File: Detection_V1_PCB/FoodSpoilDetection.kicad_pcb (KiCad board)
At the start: 2 copper layers, 60 x 65 mm, 43 parts, among them J1 Conn_01x03_Socket, J2 Conn_01x04_Socket, J3 Conn_01x06_Socket, J4 Conn_01x03_Socket, J5 Conn_01x10_Socket, J6 Conn_01x03_Socket, Q1 AO3401A, Q2 AO3400A, Q3 AO3401A, U1 XIAO-ESP32-S3-DIP

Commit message: swwe
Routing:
- net Net-(D1-K): track 95.0 -> 107.0 mm
- net GNDPWR: track 226.0 -> 221.3 mm
- net GND: vias 4 -> 2
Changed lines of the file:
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@@
+	)
+	(segment
+		(start 126.1 109.9375)
+		(end 126.1 118.205634)
+		(width 0.2)
+		(layer "F.Cu")
+		(net 13)
 	)
 	(segment
@@
 	)
 	(segment
+		(start 126.1 118.205634)
+		(end 126.4 118.505634)
+		(width 0.2)
+		(layer "F.Cu")
+		(net 13)
+	)
+	(segment
 		(start 156.75 101.310835)
 		(end 156.75 105.9829)
@@
 	)
 	(segment
+		(start 126.4 118.505634)
+		(end 126.4 121.775)
+		(width 0.2)
+		(layer "F.Cu")
+		(net 13)
+	)
+	(segment
 		(start 126.05 98.75)
 		(end 127.056847 99.756847)
@@
 	)
 	(segment
-		(start 178.816 130.048)
-		(end 177.064 131.8)
-		(width 0.2)
-		(layer "B.Cu")
-		(net 16)
-	)
-	(segment
 		(start 131.869 70.95)
 		(end 129.032 73.787)
@@
 	(segment
 		(start 126.15 127.547)
-		(end 128.778 130.175)
-		(width 0.2)
-		(layer "B.Cu")
-		(net 16)
-	)
-	(segment
-		(start 130.403 131.8)
 		(end 128.778 130.175)
 		(width 0.2)
@@
 	)
 	(via
-		(at 163.35 110.5)
-		(size 0.6)
-		(drill 0.3)
-		(layers "F.Cu" "B.Cu")
-		(net 19)
-	)
-	(via
-		(at 162.65 97.3)
-		(size 0.6)
-		(drill 0.3)
-		(layers "F.Cu" "B.Cu")
-		(net 19)
-	)
-	(via
 		(at 160.07517 103.204021)
 		(size 0.6)
@@
 	)
 	(segment
-		(start 139.865 100.387)
-		(end 137.213 100.387)
-		(width 0.2)
-		(layer "B.Cu")
-		(net 19)
-	)
-	(segment
 		(start 172.181 97.969)
 		(end 163.319 97.969)
@@
 	)
 	(segment
-		(start 140.263 100.387)
-		(end 139.865 100.387)
-		(width 0.2)
-		(layer "B.Cu")
+		(start 137.213 100.387)
+		(end 140.263 100.387)
+		(width 0.2)
+		(layer "B.Cu")

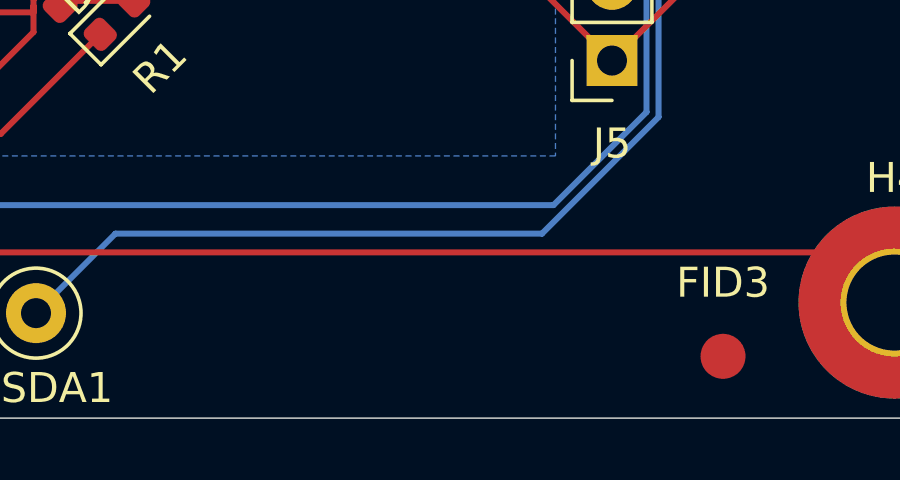
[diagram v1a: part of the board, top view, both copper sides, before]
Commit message: switch update
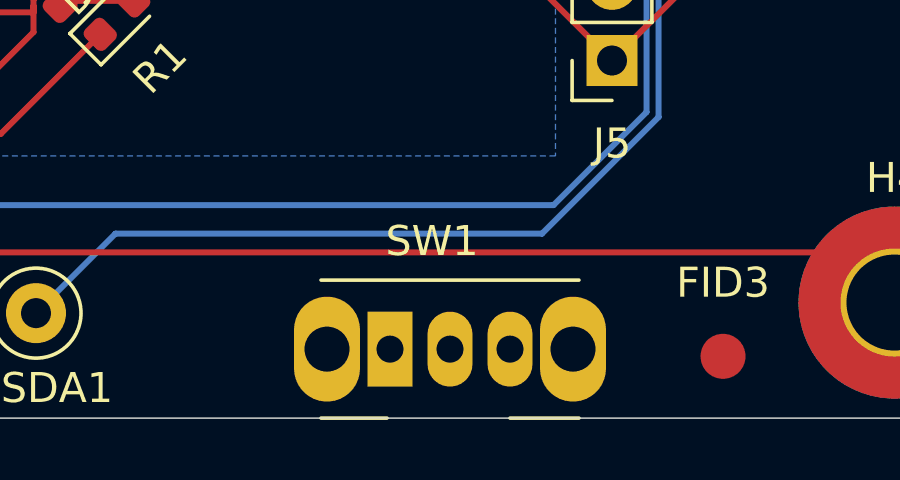
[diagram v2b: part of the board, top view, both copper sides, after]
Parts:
- added SW1: SW_DIP_x01, Button_Switch_THT:SW_Slide_SPDT_Angled_CK_OS102011MA1Q, F.Cu at (162.0, 131.6)

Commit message: so close
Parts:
- added BATTERY+1: TestPoint, TestPoint:TestPoint_Loop_D1.80mm_Drill1.0mm_Beaded, F.Cu at (138.2, 148.6)
- added BAT_SW1: TestPoint, TestPoint:TestPoint_Loop_D1.80mm_Drill1.0mm_Beaded, F.Cu at (147.0, 148.6)
- added J7: BATTERY_IN, Connector_PinHeader_2.54mm:PinHeader_1x02_P2.54mm_Vertical, F.Cu at (146.8, 138.3)
- added J8: XIAO_BAT, Connector_PinHeader_2.54mm:PinHeader_1x02_P2.54mm_Vertical, F.Cu at (151.2, 135.8)
- Q1, Q3: footprint Package_TO_SOT_SMD:SOT-23 -> A03401A:SOT-23-3L_AOS
- SW1: value SW_DIP_x01 -> SW_SPDT
- moved SDA1 12.4 mm to (139.4, 136.5)
- moved SCL1 10.4 mm to (135.2, 136.3)
- moved SW1 7.68 mm to (157.4, 137.7)
- moved FID2 7.55 mm to (130.2, 77.5)
- moved 3v1 7.50 mm to (138.4, 79.9)
- moved A1 7.50 mm to (144.8, 79.9)
- moved D2 7.50 mm to (153.0, 115.4)
- moved R7 7.50 mm to (158.9, 111.4)
- moved R6 7.50 mm to (123.3, 121.1)
- moved A3 7.50 mm to (163.4, 80.1)
- moved D1 7.50 mm to (148.9, 126.9)
- moved D5 7.50 mm to (125.4, 105.5)
- moved GND1 7.50 mm to (157.8, 80.3)
- moved J2 7.50 mm to (175.2, 99.8)
- moved J3 7.50 mm to (177.2, 88.3)
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- renumbered 3v3 to 3v1
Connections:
- H1 pad 1: GNDPWR -> GND
- H2 pad 1: GNDPWR -> GND
- H3 pad 1: GNDPWR -> GND
- H4 pad 1: GNDPWR -> GND
- J5 pad 6: GND -> unconnected-(J5-Pin_6-Pad6)
- J5 pad 7: /A0 -> unconnected-(J5-Pin_7-Pad7)
- SW1 pad 1: unconnected-(SW1-Pad1) -> /BAT_SW
- SW1 pad 2: unconnected-(SW1-Pad2) -> /BATTERY+
- SW1 pad 3: (no net) -> unconnected-(SW1-C-Pad3)
- U1 pad 10: /MISO -> unconnected-(U1-GPIO8_A9_D9_MISO-Pad10)
- U1 pad 11: /MOSI -> unconnected-(U1-GPIO9_A10_D10_MOSI-Pad11)
- U1 pad 14: 5V -> unconnected-(U1-VBUS-Pad14)
- U1 pad 4: /D3 -> unconnected-(U1-GPIO4_A3_D3-Pad4)
- U1 pad 7: /D6 -> unconnected-(U1-GPIO43_D6_TX-Pad7)
- U1 pad 8: /RX -> unconnected-(U1-GPIO44_D7_RX-Pad8)_1
- U1 pad 9: /SCK -> unconnected-(U1-GPIO7_A8_D8_SCK-Pad9)_1
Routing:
- net GNDPWR: track 221.3 -> 0.00 mm
- net GND: track 124.2 -> 287.4 mm
- net SDA: track 111.7 -> 118.5 mm
- net SCL: track 103.3 -> 107.6 mm

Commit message: finished routing
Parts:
- moved BATTERY+1 11.5 mm to (141.6, 137.7)
- moved BAT_SW1 11.0 mm to (145.4, 137.8)
- moved SW1 2.77 mm to (160.1, 137.0)
- moved J8 2.73 mm to (153.9, 136.0)
- moved J7 2.73 mm to (149.5, 138.6)
- moved SDA1 1.91 mm to (137.8, 137.6)
- moved SCL1 1.77 mm to (134.0, 137.7)
- moved J2 1.38 mm to (173.9, 99.3)
- moved R7 0.42 mm to (158.9, 111.8)
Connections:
- Q1 pad 2: GND -> 3v3
- Q3 pad 2: GND -> 3v3
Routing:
- net GND: track 287.4 -> 325.6 mm, vias 2 -> 1
- net 3v3: track 340.9 -> 375.0 mm, vias 0 -> 2
- net /BATTERY+: track 0.00 -> 22.6 mm
- net /BAT_SW: track 0.00 -> 17.0 mm
- net SDA: track 118.5 -> 125.3 mm
- net SCL: track 107.6 -> 114.4 mm
- net /A2: track 72.6 -> 75.0 mm
- net /A1: track 91.1 -> 93.5 mm
- net /A3: track 54.6 -> 56.8 mm
- net Net-(J1-Pin_2): track 38.5 -> 37.0 mm
- net D1: track 45.5 -> 46.3 mm
- net Net-(J2-Pin_1): track 24.3 -> 23.8 mm
